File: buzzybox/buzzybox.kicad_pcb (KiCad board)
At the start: 2 copper layers, 116.8 x 71.1 mm, 67 parts, among them J1 AudioJack2, J2 Barrel_Jack, Q1 Q_NPN_EBC, Q10 Q_NPN_EBC, Q2 Q_NPN_EBC, Q3 Q_NPN_EBC, Q4 Q_NPN_EBC, Q5 Q_NPN_EBC, Q6 Q_NPN_EBC, Q7 Q_NPN_EBC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

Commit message: complete mini layout
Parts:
- removed the C11 at (177.8, 87.6)
- added C1: CP1, Capacitor_THT:CP_Radial_D4.0mm_P2.00mm, F.Cu at (83.8, 66.0)
- added J3: Conn_01x03, Connector_PinHeader_2.54mm:PinHeader_1x03_P2.54mm_Horizontal, F.Cu at (73.7, 59.7)
- added J4: Conn_01x03, Connector_PinHeader_2.54mm:PinHeader_1x03_P2.54mm_Horizontal, F.Cu at (129.5, 59.7)
- C10, C2, C3, C4, C5, C6, C7, C8, C9: value C -> CP1; footprint Capacitor_THT:CP_Radial_D5.0mm_P2.50mm -> Capacitor_THT:CP_Radial_D4.0mm_P2.00mm
- J1: value AudioJack2 -> AudioJack3; footprint Connectors:Stereo_Jack_3.5mm_Switch_Ledino_KB3SPRS -> buzzybox:STX-3000
- Q1, Q10, Q2, Q3, Q4, Q5, Q6, Q7, Q8, Q9: value Q_NPN_EBC -> NPN
- moved C6 97.3 mm to (83.8, 87.6)
- moved J1 28.8 mm to (111.8, 52.1), turned to 0 degrees
- moved H2 22.7 mm to (156.2, 53.3)
- moved J2 21.7 mm to (144.8, 61.0)
- moved R9 20.7 mm to (139.7, 72.4)
- moved D5 20.7 mm to (147.3, 64.8)
- moved RV5 20.7 mm to (144.8, 82.5)
- moved R19 20.3 mm to (139.7, 94.0)
- moved D10 20.3 mm to (147.3, 86.4)
- moved RV10 20.3 mm to (144.8, 104.1)
- moved H3 20.3 mm to (156.2, 106.7)
- moved Q5 18.2 mm to (142.2, 67.3)
- moved R2 18.2 mm to (83.8, 82.5)
- moved R12 18.0 mm to (83.8, 104.1)
- moved Q10 17.7 mm to (142.3, 88.9)
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- renumbered C1 to C11
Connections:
- C11 pad 2: Net-(C1-Pad2) -> Net-(C11-Pad2)
- D1 pad 2: Net-(C2-Pad2) -> Net-(C1-Pad2)
- D10 pad 2: Net-(C11-Pad2) -> Net-(C10-Pad2)
- D2 pad 2: Net-(C3-Pad2) -> Net-(C2-Pad2)
- D3 pad 2: Net-(C4-Pad2) -> Net-(C3-Pad2)
- D4 pad 2: Net-(C5-Pad2) -> Net-(C4-Pad2)
- D5 pad 2: Net-(C6-Pad2) -> Net-(C5-Pad2)
- D6 pad 2: Net-(C7-Pad2) -> Net-(C6-Pad2)
- D7 pad 2: Net-(C8-Pad2) -> Net-(C7-Pad2)
- D8 pad 2: Net-(C9-Pad2) -> Net-(C8-Pad2)
- D9 pad 2: Net-(C10-Pad2) -> Net-(C9-Pad2)
- Q1 pad 1: Net-(C2-Pad1) -> Net-(C1-Pad1)
- Q1 pad 3: Net-(C2-Pad2) -> Net-(C1-Pad2)
- Q10 pad 1: Net-(C11-Pad1) -> Net-(C10-Pad1)
- Q10 pad 3: Net-(C11-Pad2) -> Net-(C10-Pad2)
- Q2 pad 1: Net-(C3-Pad1) -> Net-(C2-Pad1)
- Q2 pad 3: Net-(C3-Pad2) -> Net-(C2-Pad2)
- Q3 pad 1: Net-(C4-Pad1) -> Net-(C3-Pad1)
- Q3 pad 3: Net-(C4-Pad2) -> Net-(C3-Pad2)
- Q4 pad 1: Net-(C5-Pad1) -> Net-(C4-Pad1)
- Q4 pad 3: Net-(C5-Pad2) -> Net-(C4-Pad2)
- Q5 pad 1: Net-(C6-Pad1) -> Net-(C5-Pad1)
- Q5 pad 3: Net-(C6-Pad2) -> Net-(C5-Pad2)
- Q6 pad 1: Net-(C7-Pad1) -> Net-(C6-Pad1)
- Q6 pad 3: Net-(C7-Pad2) -> Net-(C6-Pad2)
- Q7 pad 1: Net-(C8-Pad1) -> Net-(C7-Pad1)
- Q7 pad 3: Net-(C8-Pad2) -> Net-(C7-Pad2)
- Q8 pad 1: Net-(C9-Pad1) -> Net-(C8-Pad1)
- Q8 pad 3: Net-(C9-Pad2) -> Net-(C8-Pad2)
- Q9 pad 1: Net-(C10-Pad1) -> Net-(C9-Pad1)
- Q9 pad 3: Net-(C10-Pad2) -> Net-(C9-Pad2)
- R10 pad 2: Net-(C6-Pad1) -> Net-(C5-Pad1)
- R12 pad 2: Net-(C7-Pad1) -> Net-(C6-Pad1)
- R14 pad 2: Net-(C8-Pad1) -> Net-(C7-Pad1)
- R16 pad 2: Net-(C9-Pad1) -> Net-(C8-Pad1)
- R18 pad 2: Net-(C10-Pad1) -> Net-(C9-Pad1)
- R2 pad 2: Net-(C2-Pad1) -> Net-(C1-Pad1)
- R20 pad 2: Net-(C11-Pad1) -> Net-(C10-Pad1)
- R4 pad 2: Net-(C3-Pad1) -> Net-(C2-Pad1)
- R6 pad 2: Net-(C4-Pad1) -> Net-(C3-Pad1)
- R8 pad 2: Net-(C5-Pad1) -> Net-(C4-Pad1)
- RV1 pad 3: Net-(C2-Pad1) -> Net-(C1-Pad1)
- RV10 pad 3: Net-(C11-Pad1) -> Net-(C10-Pad1)
- RV2 pad 3: Net-(C3-Pad1) -> Net-(C2-Pad1)
- RV3 pad 3: Net-(C4-Pad1) -> Net-(C3-Pad1)
- RV4 pad 3: Net-(C5-Pad1) -> Net-(C4-Pad1)
- RV5 pad 3: Net-(C6-Pad1) -> Net-(C5-Pad1)
- RV6 pad 3: Net-(C7-Pad1) -> Net-(C6-Pad1)
- RV7 pad 3: Net-(C8-Pad1) -> Net-(C7-Pad1)
- RV8 pad 3: Net-(C9-Pad1) -> Net-(C8-Pad1)
- RV9 pad 3: Net-(C10-Pad1) -> Net-(C9-Pad1)
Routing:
- net Net-(C11-Pad1): track 46.2 -> 0.00 mm
- net Net-(C11-Pad2): track 16.8 -> 63.0 mm
- net Net-(C1-Pad1): track 0.00 -> 34.3 mm
- net /oscillator/OSC_OUT: track 223.6 -> 209.8 mm
- net Net-(C1-Pad2): track 0.00 -> 12.3 mm
- net Net-(C9-Pad1): track 46.2 -> 34.3 mm
- net Net-(C10-Pad1): track 46.2 -> 34.3 mm
- net Net-(C8-Pad1): track 46.2 -> 34.3 mm
- net Net-(C2-Pad1): track 46.2 -> 34.3 mm
- net Net-(C3-Pad1): track 46.2 -> 34.3 mm
- net Net-(C4-Pad1): track 46.2 -> 34.3 mm
- net Net-(C6-Pad1): track 46.2 -> 34.4 mm
- net Net-(C5-Pad1): track 46.1 -> 34.3 mm
- net Net-(C7-Pad1): track 44.7 -> 34.3 mm
- net +VDC: track 235.2 -> 225.9 mm
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- added copper zone on F.Cu, net -VDC
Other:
- board size 116.8 x 71.1 mm -> 96.6 x 61 mm
- board text added: "+VDC GND AUD"
- board text added: "JLCJLCJLCJLC"

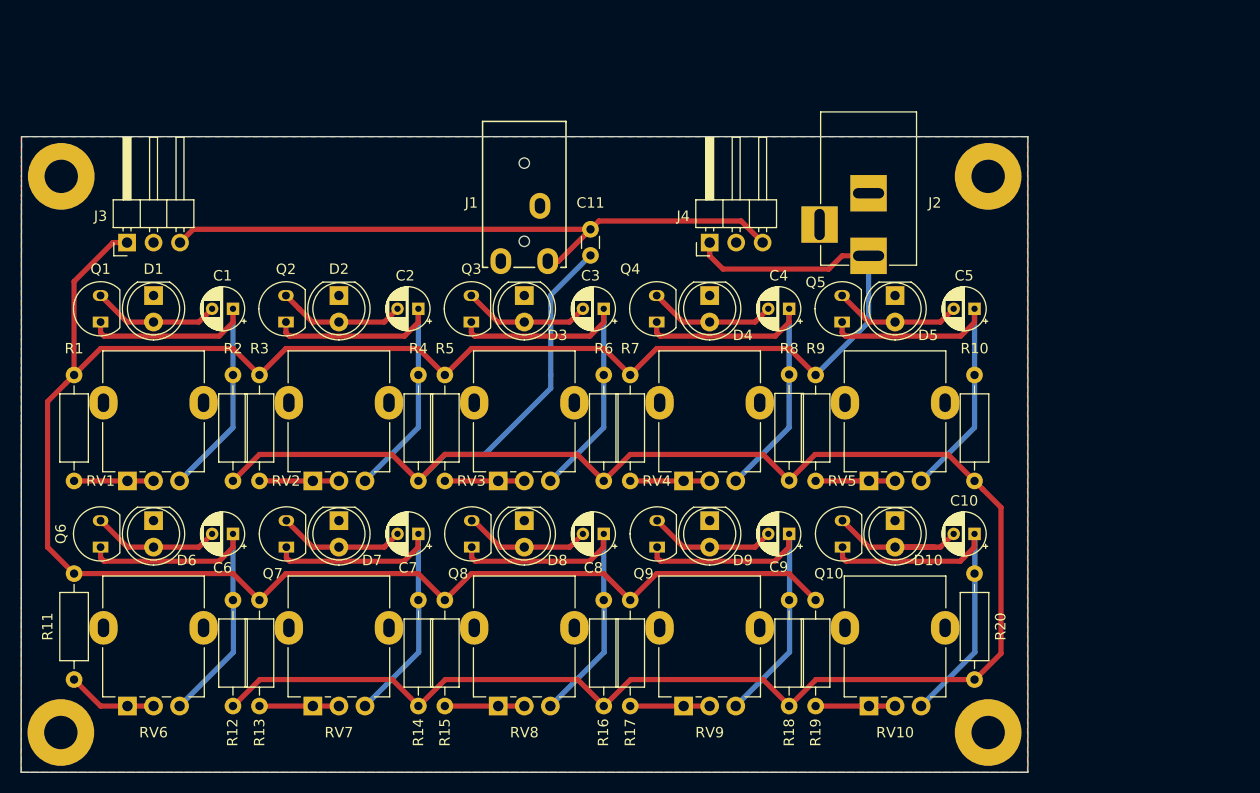
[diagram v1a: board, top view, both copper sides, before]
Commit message: finalize main PCB after parts recieved
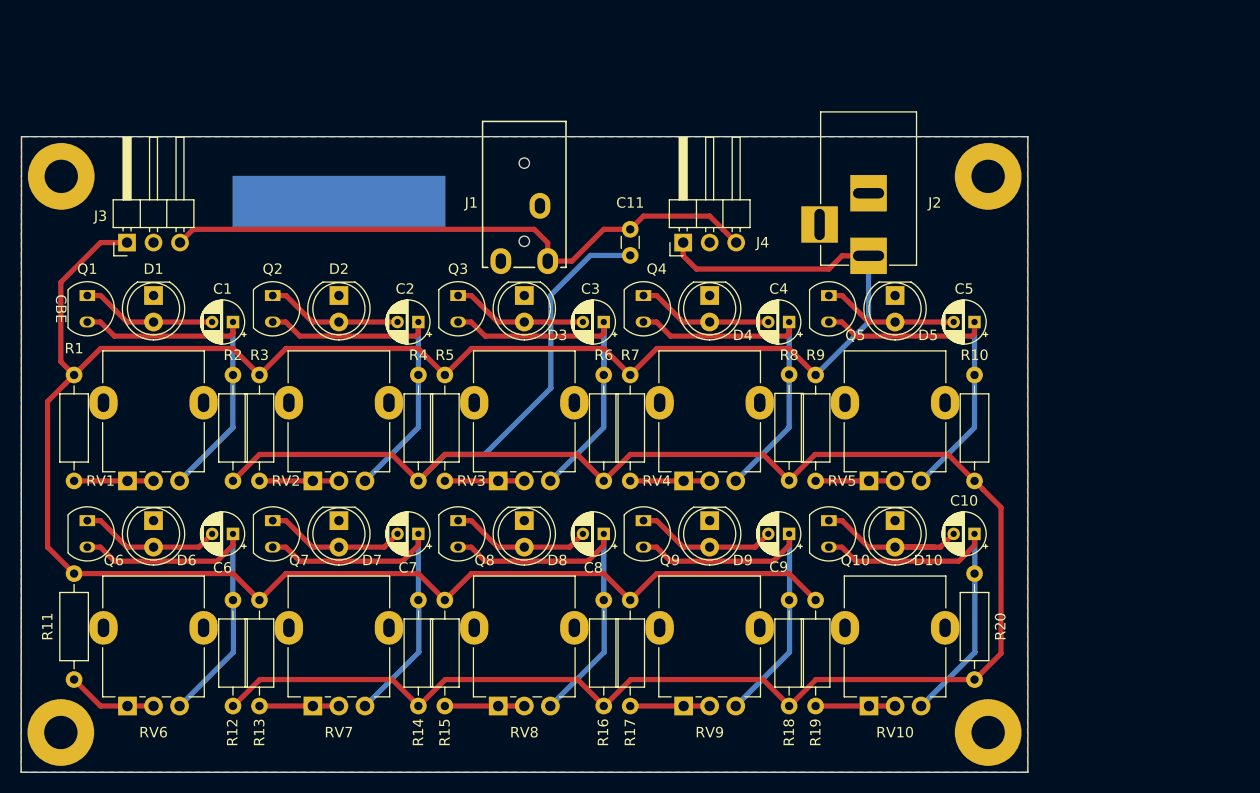
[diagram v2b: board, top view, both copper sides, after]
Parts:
- Q1, Q10, Q2, Q3, Q4, Q5, Q6, Q7, Q8, Q9: value NPN -> Q_NPN_CBE
- moved C11 3.81 mm to (121.9, 60.9)
- moved Q10 2.86 mm to (141.0, 86.4), turned to 270 degrees
- moved Q7 2.86 mm to (87.6, 86.4), turned to 270 degrees
- moved Q8 2.86 mm to (105.4, 86.4), turned to 270 degrees
- moved Q9 2.86 mm to (123.2, 86.4), turned to 270 degrees
- moved Q1 2.84 mm to (69.8, 64.8), turned to 270 degrees
- moved Q2 2.84 mm to (87.6, 64.8), turned to 270 degrees
- moved Q3 2.84 mm to (105.4, 64.8), turned to 270 degrees
- moved Q5 2.84 mm to (141.0, 64.8), turned to 270 degrees
- moved Q6 2.84 mm to (69.8, 86.4), turned to 270 degrees
- moved Q4 2.84 mm to (123.2, 64.8), turned to 270 degrees
- moved J4 2.54 mm to (127.0, 59.7)
- moved C1 1.27 mm to (83.8, 67.3)
- moved C2 1.27 mm to (101.6, 67.3)
- moved C3 1.27 mm to (119.4, 67.3)
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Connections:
- net -VDC renamed GND
- Q1 pad 1: Net-(C1-Pad1) -> Net-(C1-Pad2)
- Q1 pad 3: Net-(C1-Pad2) -> Net-(C1-Pad1)
- Q10 pad 1: Net-(C10-Pad1) -> Net-(C10-Pad2)
- Q10 pad 3: Net-(C10-Pad2) -> Net-(C10-Pad1)
- Q2 pad 1: Net-(C2-Pad1) -> Net-(C2-Pad2)
- Q2 pad 3: Net-(C2-Pad2) -> Net-(C2-Pad1)
- Q3 pad 1: Net-(C3-Pad1) -> Net-(C3-Pad2)
- Q3 pad 3: Net-(C3-Pad2) -> Net-(C3-Pad1)
- Q4 pad 1: Net-(C4-Pad1) -> Net-(C4-Pad2)
- Q4 pad 3: Net-(C4-Pad2) -> Net-(C4-Pad1)
- Q5 pad 1: Net-(C5-Pad1) -> Net-(C5-Pad2)
- Q5 pad 3: Net-(C5-Pad2) -> Net-(C5-Pad1)
- Q6 pad 1: Net-(C6-Pad1) -> Net-(C6-Pad2)
- Q6 pad 3: Net-(C6-Pad2) -> Net-(C6-Pad1)
- Q7 pad 1: Net-(C7-Pad1) -> Net-(C7-Pad2)
- Q7 pad 3: Net-(C7-Pad2) -> Net-(C7-Pad1)
- Q8 pad 1: Net-(C8-Pad1) -> Net-(C8-Pad2)
- Q8 pad 3: Net-(C8-Pad2) -> Net-(C8-Pad1)
- Q9 pad 1: Net-(C9-Pad1) -> Net-(C9-Pad2)
- Q9 pad 3: Net-(C9-Pad2) -> Net-(C9-Pad1)
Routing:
- net +VDC: track 225.9 -> 230.2 mm
- net /oscillator/OSC_OUT: track 209.8 -> 213.6 mm
- net Net-(C3-Pad1): track 34.3 -> 38.1 mm
- net Net-(C11-Pad2): track 63.0 -> 59.2 mm
- net Net-(C7-Pad2): track 12.2 -> 13.5 mm
- net Net-(C6-Pad2): track 12.2 -> 13.5 mm
- net Net-(C9-Pad2): track 12.2 -> 13.5 mm
- net Net-(C10-Pad2): track 16.0 -> 17.4 mm
- net Net-(C8-Pad2): track 12.3 -> 13.5 mm
- net Net-(C4-Pad1): track 34.3 -> 33.1 mm
- net Net-(C5-Pad1): track 34.3 -> 33.1 mm
- net Net-(C2-Pad1): track 34.3 -> 33.1 mm
- net Net-(C1-Pad1): track 34.3 -> 33.1 mm
- net Net-(C5-Pad2): track 12.3 -> 13.0 mm
- net Net-(C3-Pad2): track 12.3 -> 13.0 mm
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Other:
- board text added: "CBE"
- board text added: "Max Proskauer v0.1 Dec 2020"
- board text added: "SN"
- board text added: "TODO: - Check transistor pinout"
- board text added: "https://github.com/mprosk/buzzybox"

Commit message: complete refit
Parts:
- moved C10 17.3 mm to (137.7, 85.7), turned to 0 degrees
- moved C7 17.3 mm to (84.4, 85.7), turned to 0 degrees
- moved Q10 12.7 mm to (153.7, 86.4)
- moved Q7 4.02 mm to (88.9, 90.2), turned to 90 degrees
- moved C6 3.75 mm to (85.8, 90.8)
- moved C8 3.75 mm to (121.4, 90.8)
- moved C9 3.75 mm to (139.2, 90.8)
- moved Q9 1.42 mm to (124.5, 85.7), turned to 180 degrees
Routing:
- net Net-(C8-Pad1): track 34.9 -> 32.4 mm
- net Net-(C6-Pad1): track 34.9 -> 32.4 mm
- net Net-(C7-Pad2): track 13.5 -> 11.2 mm
- net Net-(C8-Pad2): track 13.5 -> 15.8 mm
- net Net-(C6-Pad2): track 13.5 -> 15.8 mm
- net Net-(C10-Pad1): track 34.9 -> 37.0 mm
- net Net-(C10-Pad2): track 17.4 -> 18.9 mm
- net +VDC: track 230.2 -> 228.7 mm
- net Net-(C7-Pad1): track 34.9 -> 33.6 mm
- net Net-(C9-Pad2): track 13.5 -> 14.8 mm

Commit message: Update to KiCAD6 and created schematic PDF
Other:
- net class Default removed
